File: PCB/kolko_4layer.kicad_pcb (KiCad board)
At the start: 4 copper layers, 141.4 x 141.4 mm, 82 parts, among them IC1 74HC4067PW-Q100J, J1 USB_C_Receptacle_USB2.0_16P, J2 Conn_01x02_Socket, J3 Conn_01x04_Socket, SW1 RST, SW2 BOOT, U1 ESP32-S3-WROOM-1, U2 USBLC6-2SC6, U3 AMS1117-3.3

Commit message: routing of microphones
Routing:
- net /BCLKA: track 0.00 -> 233.3 mm, vias 0 -> 3
- net /WSA: track 0.00 -> 217.3 mm, vias 0 -> 3
- net /DATAA: track 0.00 -> 211.7 mm, vias 0 -> 3
- net /DATAB: track 0.00 -> 156.8 mm, vias 0 -> 3
- net /BCLKB: track 0.00 -> 143.3 mm, vias 0 -> 3
- net /WSB: track 0.00 -> 139.7 mm, vias 0 -> 4
- net Net-(U1-IO11): track 0.00 -> 7.73 mm
- net Net-(U1-IO10): track 0.00 -> 7.48 mm
- net Net-(U1-IO42): track 0.00 -> 4.18 mm
- net Net-(U1-IO1): track 0.00 -> 4.15 mm
- net Net-(MK4-DATA): track 0.00 -> 3.98 mm
- net Net-(MK1-DATA): track 0.00 -> 3.16 mm
- net Net-(MK2-DATA): track 0.00 -> 3.13 mm
- net Net-(MK3-DATA): track 0.00 -> 2.51 mm
- net (no net): vias 0 -> 1

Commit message: buttons and pwr supply
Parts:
- moved R6 4.50 mm to (146.5, 126.5)
- moved SW2 4.45 mm to (148.6, 131.5)
- moved U3 0.50 mm to (155.0, 149.5)
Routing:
- net VBUS: track 19.2 -> 80.9 mm
- net /ENS/RST: track 0.00 -> 49.5 mm, vias 0 -> 2
- net /BOOTS: track 0.00 -> 35.5 mm
- net VSUP: track 0.00 -> 27.0 mm, vias 0 -> 2
- net /VEXT: track 0.00 -> 25.6 mm
- net +3.3V: track 0.00 -> 21.0 mm
- net (no net): vias 1 -> 0

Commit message: buttons and stuff
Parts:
- moved C16 11.8 mm to (144.0, 80.0), turned to 90 degrees
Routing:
- net +3.3V: track 21.0 -> 142.8 mm
- net Net-(D3-A): track 0.00 -> 9.55 mm
- net Net-(D16-A): track 0.00 -> 3.97 mm
- net Net-(D8-A): track 0.00 -> 3.93 mm
- net Net-(D5-A): track 0.00 -> 3.91 mm
- net Net-(D15-A): track 0.00 -> 3.81 mm
- net Net-(D6-A): track 0.00 -> 3.76 mm
- net Net-(D11-A): track 0.00 -> 3.70 mm
- net Net-(D12-A): track 0.00 -> 3.70 mm
- net Net-(D19-A): track 0.00 -> 3.69 mm
- net Net-(D20-A): track 0.00 -> 3.66 mm
- net Net-(D14-A): track 0.00 -> 3.64 mm
- net Net-(D18-A): track 0.00 -> 3.58 mm
- net Net-(D7-A): track 0.00 -> 3.55 mm
- net Net-(D13-A): track 0.00 -> 3.45 mm
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
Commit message: leds routing
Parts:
- moved R25 0.50 mm to (161.5, 105.0), turned to 180 degrees
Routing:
- net /Y8: track 0.00 -> 121.1 mm
- net /Y7: track 0.00 -> 97.6 mm
- net /ESP_RX: track 0.00 -> 95.2 mm
- net /ESP_TX: track 0.00 -> 87.9 mm
- net /Y9: track 0.00 -> 84.7 mm, vias 0 -> 2
- net /Y6: track 0.00 -> 83.4 mm
- net /Y10: track 0.00 -> 75.1 mm, vias 0 -> 2
- net /Y5: track 0.00 -> 70.6 mm
- net /S0ESP: track 0.00 -> 68.1 mm, vias 0 -> 2
- net /Y11: track 0.00 -> 66.6 mm, vias 0 -> 2
- net /S1ESP: track 0.00 -> 62.9 mm, vias 0 -> 2
- net /Y12: track 0.00 -> 57.5 mm, vias 0 -> 2
- net /Y4: track 0.00 -> 55.9 mm
- net /EMUX: track 0.00 -> 50.4 mm
- net /S3ESP: track 0.00 -> 50.2 mm, vias 0 -> 2
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
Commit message: power
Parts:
- turned R23 to 180 degrees
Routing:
- net +3.3V: track 137.5 -> 1024.5 mm, vias 0 -> 23
- net Net-(D9-A): track 3.41 -> 4.34 mm

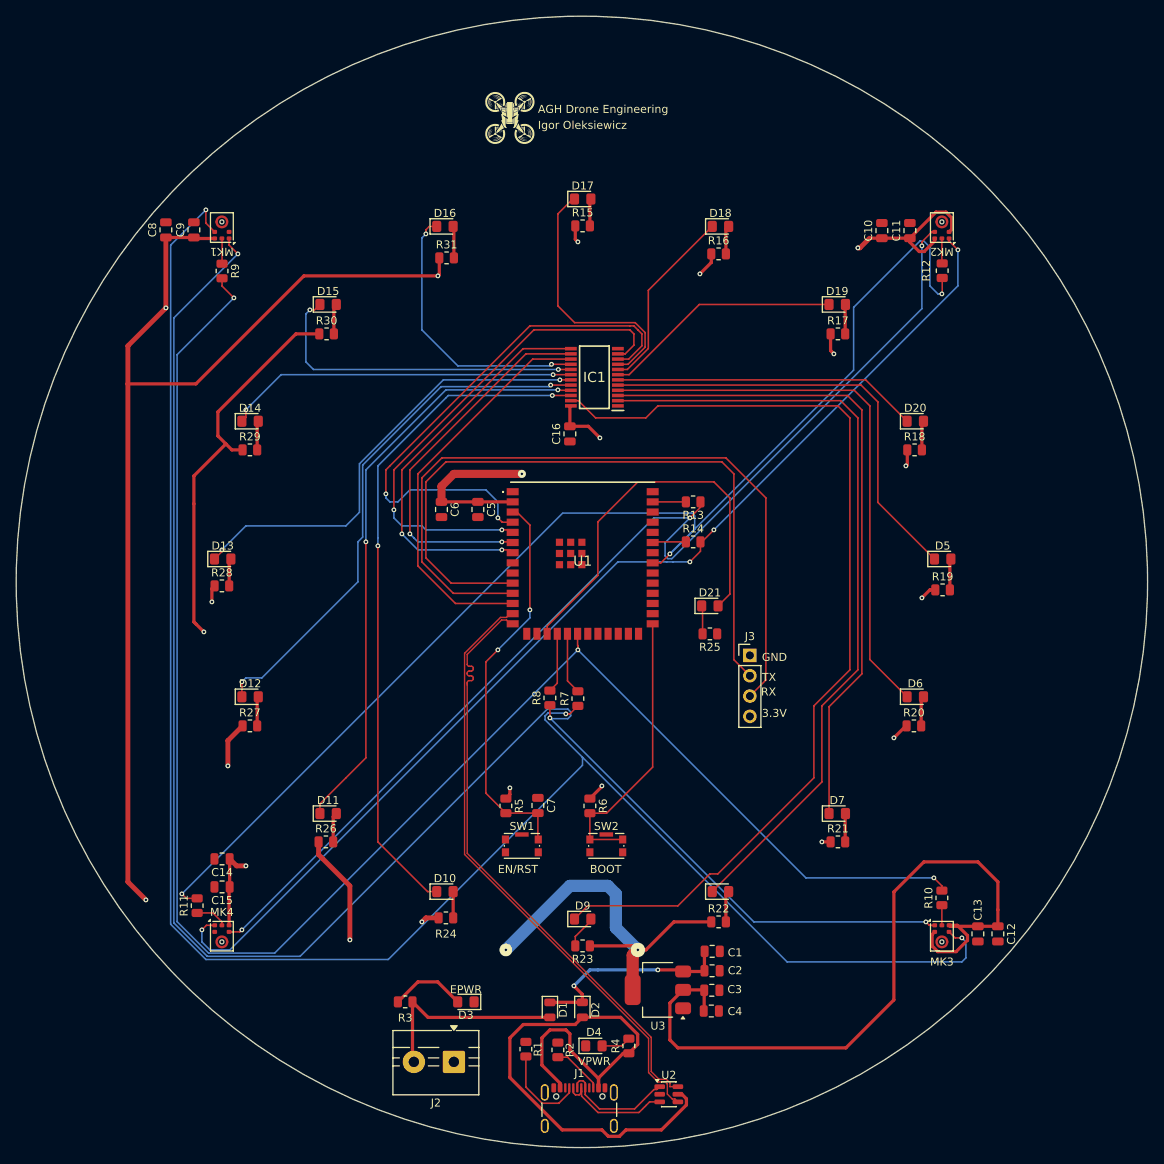
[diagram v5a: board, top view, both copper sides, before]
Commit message: add GND without stichets
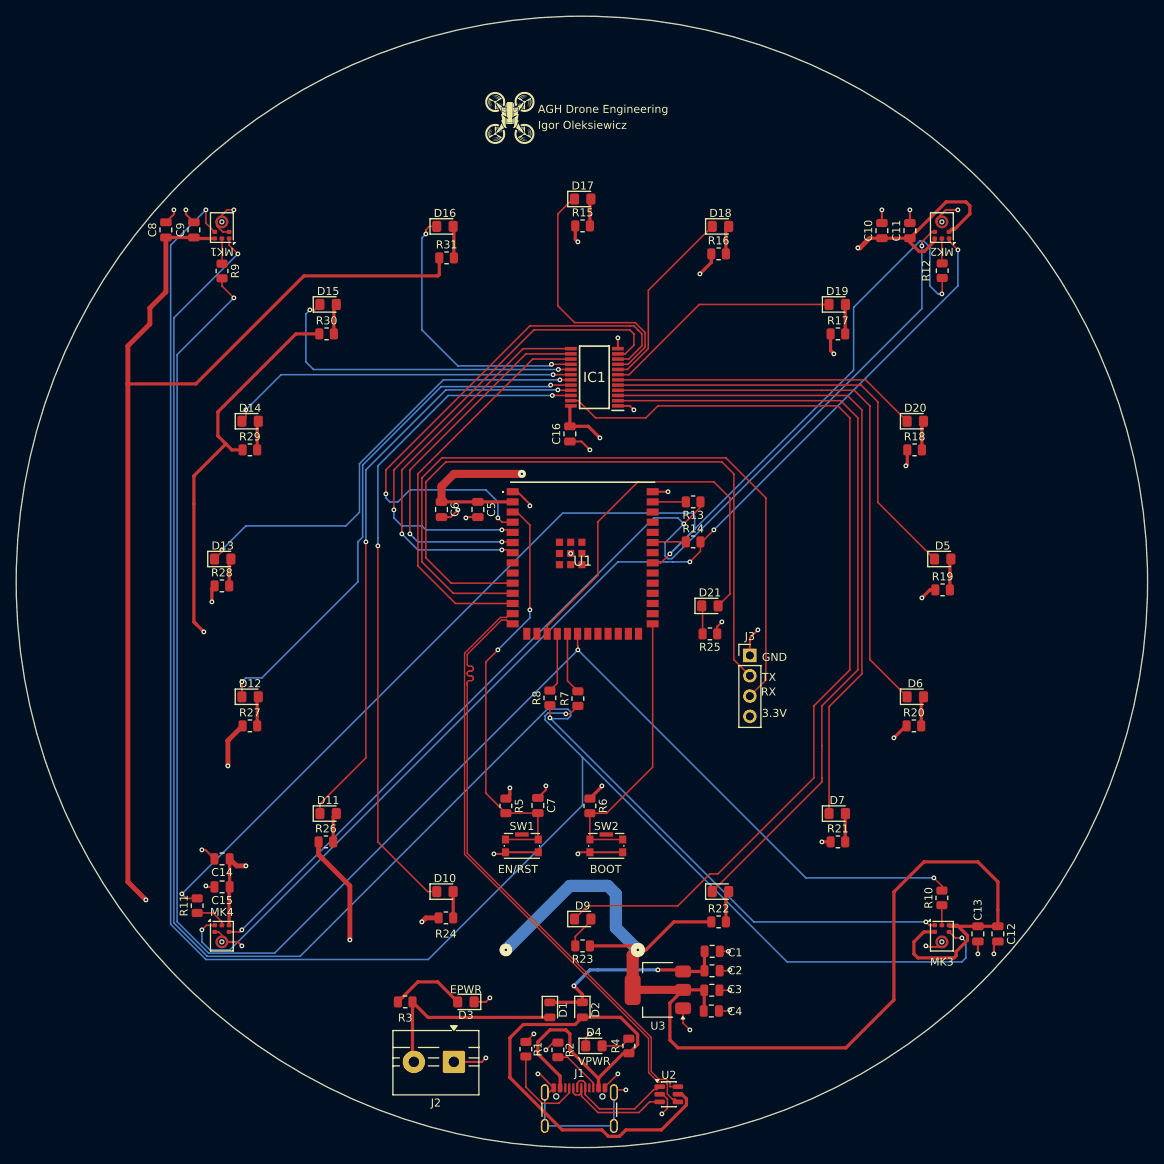
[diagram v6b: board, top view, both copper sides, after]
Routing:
- net GND: track 0.00 -> 112.7 mm, vias 0 -> 39
- net +3.3V: track 1024.5 -> 1046.4 mm, vias 23 -> 21
- net /ENS/RST: track 49.5 -> 53.6 mm
- net /BCLKA: track 233.8 -> 236.8 mm
- added copper zone on In1.Cu, net GND
- added copper zone on In2.Cu, net GND

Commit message: add GND stiching
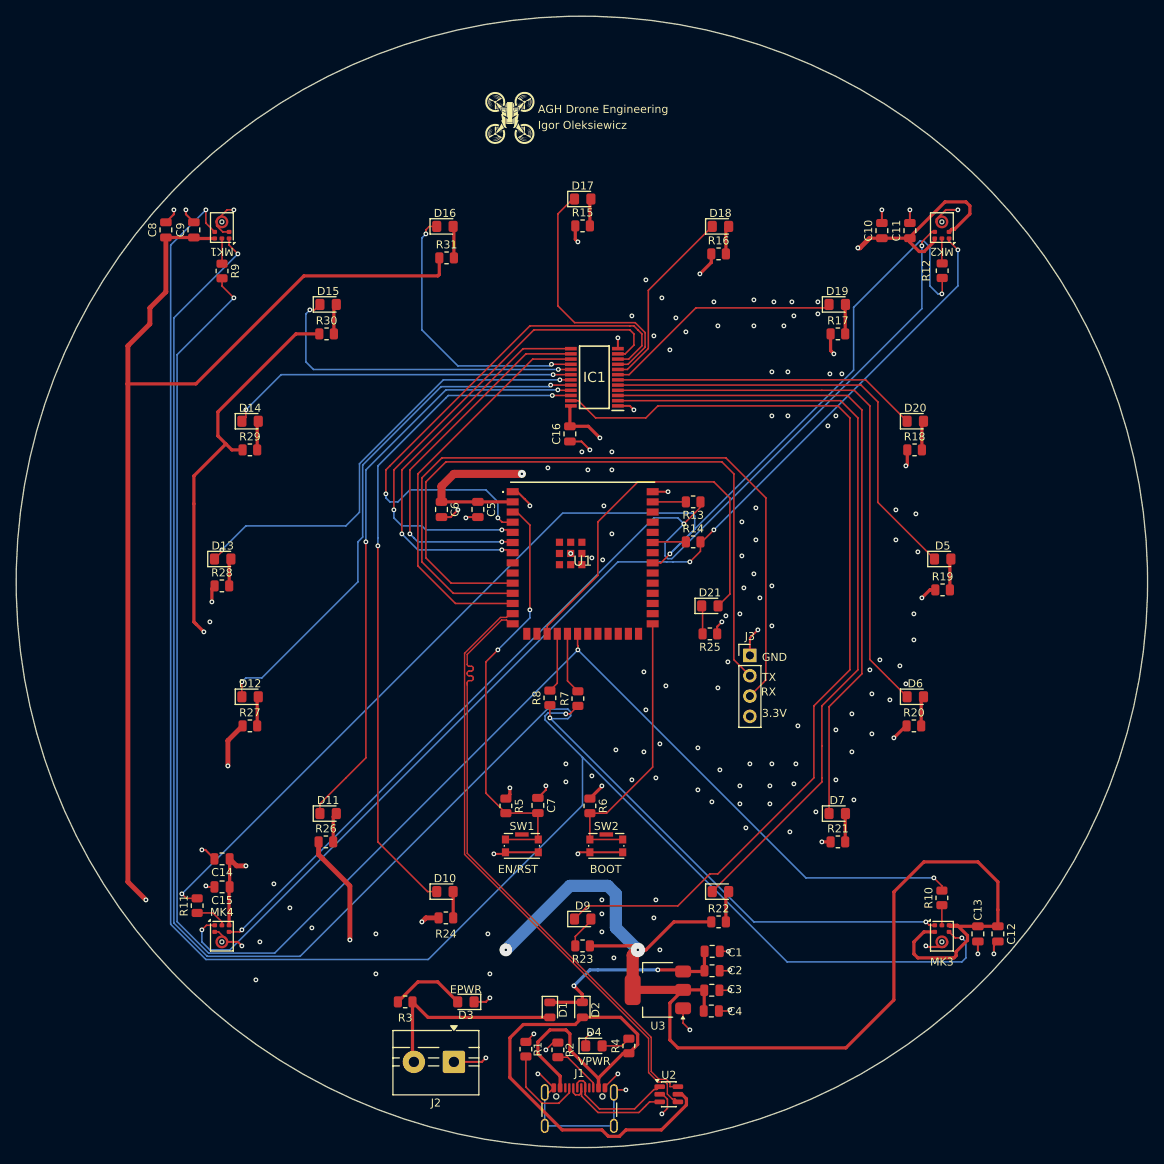
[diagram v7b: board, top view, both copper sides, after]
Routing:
- net +3.3V: track 1046.4 -> 991.4 mm
- net GND: vias 39 -> 148

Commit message: usb reroute
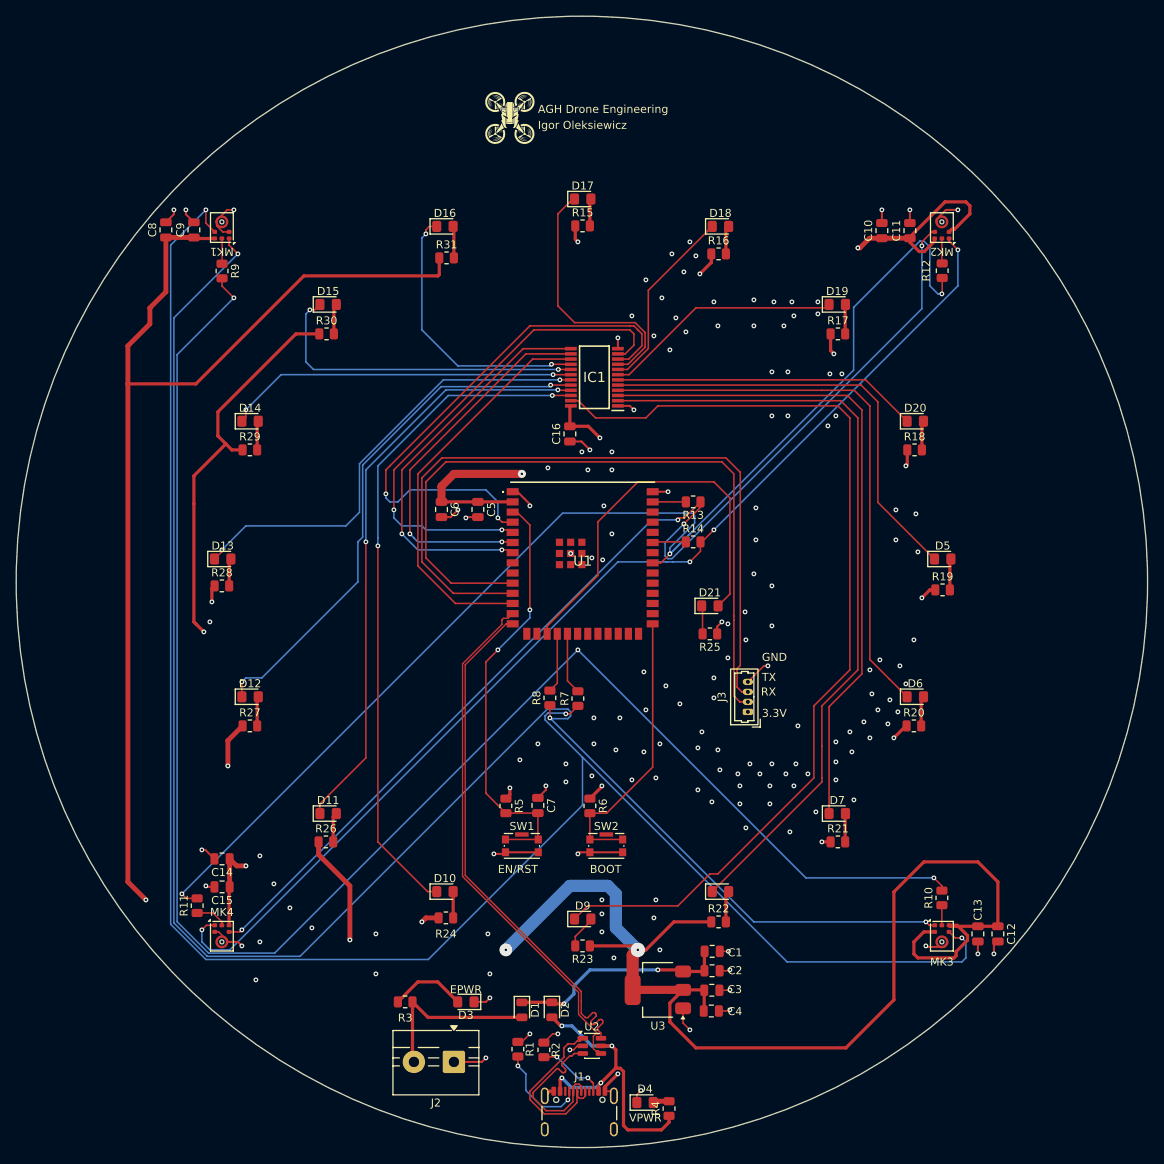
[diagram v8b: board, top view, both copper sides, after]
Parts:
- J3: footprint Connector_PinHeader_2.54mm:PinHeader_1x04_P2.54mm_Vertical -> Connector_Molex:Molex_PicoBlade_53047-0410_1x04_P1.25mm_Vertical
- moved U2 11.4 mm to (146.8, 156.5)
- moved D4 9.54 mm to (153.4, 163.6)
- moved R4 9.30 mm to (156.4, 164.3)
- moved J3 7.06 mm to (166.2, 114.8), turned to 90 degrees
- moved D2 3.81 mm to (141.8, 152.0)
- moved D1 3.50 mm to (138.0, 152.0)
- moved R2 1.75 mm to (140.8, 157.0)
- moved R1 1.00 mm to (137.5, 156.9)
- moved J1 0.42 mm to (145.2, 165.8)
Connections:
- J3 pad 1: GND -> +3.3V
- J3 pad 4: +3.3V -> GND
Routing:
- net +3.3V: track 991.4 -> 915.0 mm
- net VBUS: track 81.3 -> 39.5 mm, vias 0 -> 4
- net GND: track 112.7 -> 92.9 mm, vias 148 -> 165
- net /D_1MCU+: track 75.8 -> 66.2 mm
- net /D_1MCU-: track 75.9 -> 66.3 mm
- net /D_1+: track 14.5 -> 23.0 mm
- net /D_1-: track 14.7 -> 20.8 mm
- net /DATAB: track 157.1 -> 161.5 mm
- net /ESP_TX: track 87.9 -> 91.6 mm
- net /VEXT: track 25.6 -> 22.1 mm
- net /BCLKB: track 142.8 -> 145.4 mm, vias 3 -> 4
- net Net-(J1-CC2): track 6.37 -> 8.73 mm, vias 0 -> 2
- net /DATAA: track 211.7 -> 209.7 mm
- net Net-(D4-A): track 3.72 -> 2.04 mm
- net VSUP: track 27.0 -> 28.6 mm
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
